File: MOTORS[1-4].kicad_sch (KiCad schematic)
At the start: 5 parts, among them U22 ZX-SH1.0-8PWT

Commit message: BME280
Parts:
- added TP10, TP3, TP4, TP5, TP6, TP7, TP8, TP9: (no value), EasyEDA:TestPoint_Pad_1.8x0.9mm, symbol Connector:TestPoint
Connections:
- net ADC_CURR1: now also TP3.1
- net GND: now also TP10.1
- net MOTOR1: now also TP5.1
- net MOTOR2: now also TP6.1
- net MOTOR3: now also TP7.1
- net MOTOR4: now also TP8.1
- net UART8.RX: now also TP4.1
- net VBAT: now also TP9.1
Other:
- moved on the sheet: R42, R43, R44, R45

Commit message: power routing
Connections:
- net MOTOR1: no longer TP5.1
- net MOTOR2: no longer TP6.1
- net MOTOR3: no longer TP7.1
- net MOTOR4: no longer TP8.1
- net S1: now also TP5.1
- net S2: now also TP6.1
- net S3: now also TP7.1
- net S4: now also TP8.1
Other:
- moved on the sheet: R42, R43, R44, R45

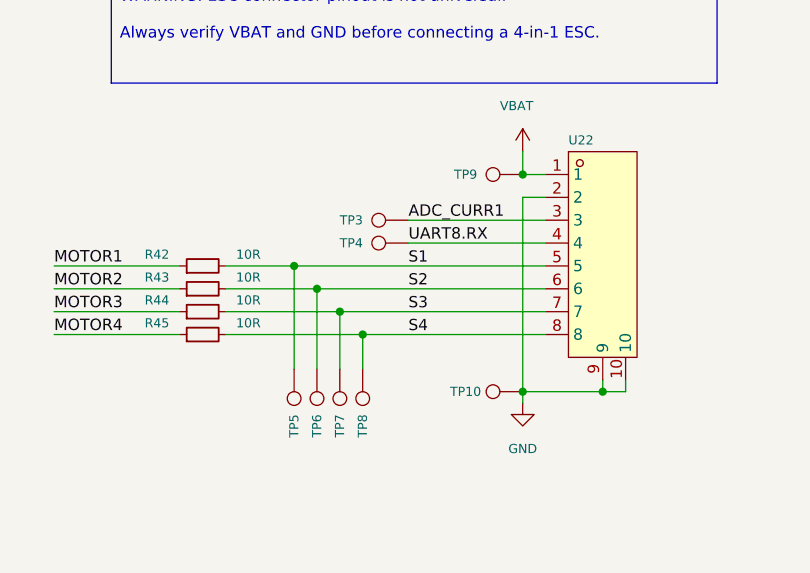
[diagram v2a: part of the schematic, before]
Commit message: BOM LCSC numbers assigned
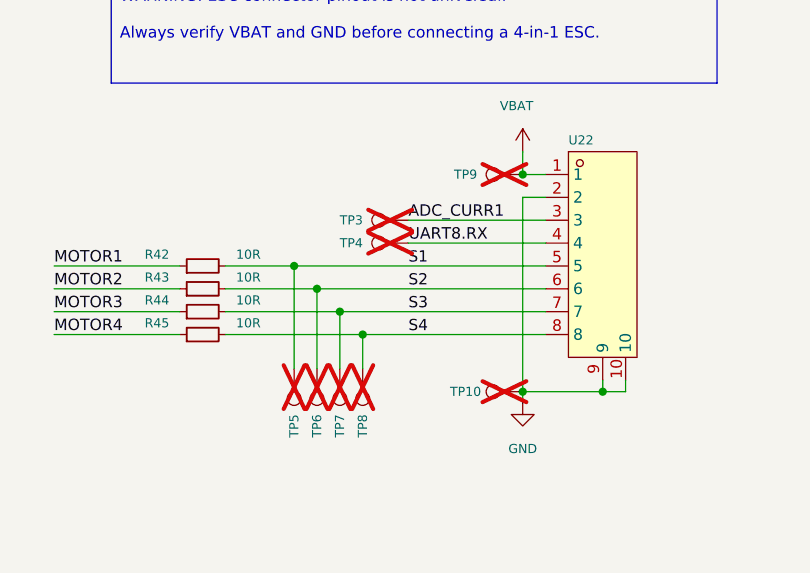
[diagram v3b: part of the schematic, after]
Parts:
- R42, R43, R44, R45: LCSC Part (none) -> C25077
- TP10, TP3, TP4, TP5, TP6, TP7, TP8, TP9: now not fitted; now left out of the parts list
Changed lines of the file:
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@@
 		(body_style 1)
 		(exclude_from_sim no)
-		(in_bom yes)
-		(on_board yes)
-		(in_pos_files yes)
-		(dnp no)
+		(in_bom no)
+		(on_board no)
+		(in_pos_files yes)
+		(dnp yes)
 		(property "Reference" "TP5"
 			(at 88.9 78.74 90)
@@
 			)
 		)
+		(property "LCSC Part" "C25077"
+			(at 78.74 60.96 90)
+			(hide yes)
+			(show_name no)
+			(do_not_autoplace no)
+			(effects
+				(font
+					(size 1.27 1.27)
+				)
+			)
+		)
 		(pin "2"
 		)
@@
 		(body_style 1)
 		(exclude_from_sim no)
-		(in_bom yes)
-		(on_board yes)
-		(in_pos_files yes)
-		(dnp no)
+		(in_bom no)
+		(on_board no)
+		(in_pos_files yes)
+		(dnp yes)
 		(property "Reference" "TP9"
 			(at 107.95 50.8 90)
@@
 			)
 		)
+		(property "LCSC Part" "C25077"
+			(at 78.74 66.04 90)
+			(hide yes)
+			(show_name no)
+			(do_not_autoplace no)
+			(effects
+				(font
+					(size 1.27 1.27)
+				)
+			)
+		)
 		(pin "2"
 		)
@@
 			)
 		)
+		(property "LCSC Part" "C25077"
+			(at 78.74 68.58 90)
+			(hide yes)
+			(show_name no)
+			(do_not_autoplace no)
+			(effects
+				(font
+					(size 1.27 1.27)
+				)
+			)
+		)
 		(pin "2"
 		)
@@
 		(body_style 1)
 		(exclude_from_sim no)
-		(in_bom yes)
-		(on_board yes)
-		(in_pos_files yes)
-		(dnp no)
+		(in_bom no)
+		(on_board no)
+		(in_pos_files yes)
+		(dnp yes)
 		(property "Reference" "TP3"
 			(at 95.25 55.88 90)
@@
 		(body_style 1)
 		(exclude_from_sim no)
-		(in_bom yes)
-		(on_board yes)
-		(in_pos_files yes)
-		(dnp no)
+		(in_bom no)
+		(on_board no)
+		(in_pos_files yes)
+		(dnp yes)
 		(property "Reference" "TP4"
 			(at 95.25 58.42 90)
@@
 		(body_style 1)
 		(exclude_from_sim no)
-		(in_bom yes)
-		(on_board yes)
-		(in_pos_files yes)
-		(dnp no)
+		(in_bom no)
+		(on_board no)
+		(in_pos_files yes)
+		(dnp yes)
 		(property "Reference" "TP7"
 			(at 93.98 78.74 90)
@@
 		(body_style 1)
 		(exclude_from_sim no)
-		(in_bom yes)
-		(on_board yes)
-		(in_pos_files yes)
-		(dnp no)
+		(in_bom no)
+		(on_board no)
+		(in_pos_files yes)
+		(dnp yes)
 		(property "Reference" "TP10"
 			(at 107.95 74.93 90)
@@
 			)
 		)
+		(property "LCSC Part" "C25077"
+			(at 78.74 63.5 90)
+			(hide yes)
+			(show_name no)
+			(do_not_autoplace no)
+			(effects
+				(font
+					(size 1.27 1.27)
+				)
+			)
+		)
 		(pin "2"
 		)
@@
 		(body_style 1)
 		(exclude_from_sim no)
-		(in_bom yes)
-		(on_board yes)
-		(in_pos_files yes)
-		(dnp no)
+		(in_bom no)
+		(on_board no)
+		(in_pos_files yes)
+		(dnp yes)
 		(property "Reference" "TP8"
 			(at 96.52 78.74 90)
@@
 		(body_style 1)
 		(exclude_from_sim no)
-		(in_bom yes)
-		(on_board yes)
-		(in_pos_files yes)
-		(dnp no)
+		(in_bom no)
+		(on_board no)
+		(in_pos_files yes)
+		(dnp yes)
 		(property "Reference" "TP6"
 			(at 91.44 78.74 90)
